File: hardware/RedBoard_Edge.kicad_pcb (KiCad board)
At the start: 2 copper layers, 101.6 x 38.1 mm, 67 parts, among them IC3 LM1117, J1 CONN_025MM, J17 Qwiic_Connector, J18 Qwiic_Connector, J2 ICSP, J3 POWER_JACKSUPER_BOMB_DIGITY, J4 microB, J5 CONN_04, J6 CONN_04, Q1 1A/60V/500mO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

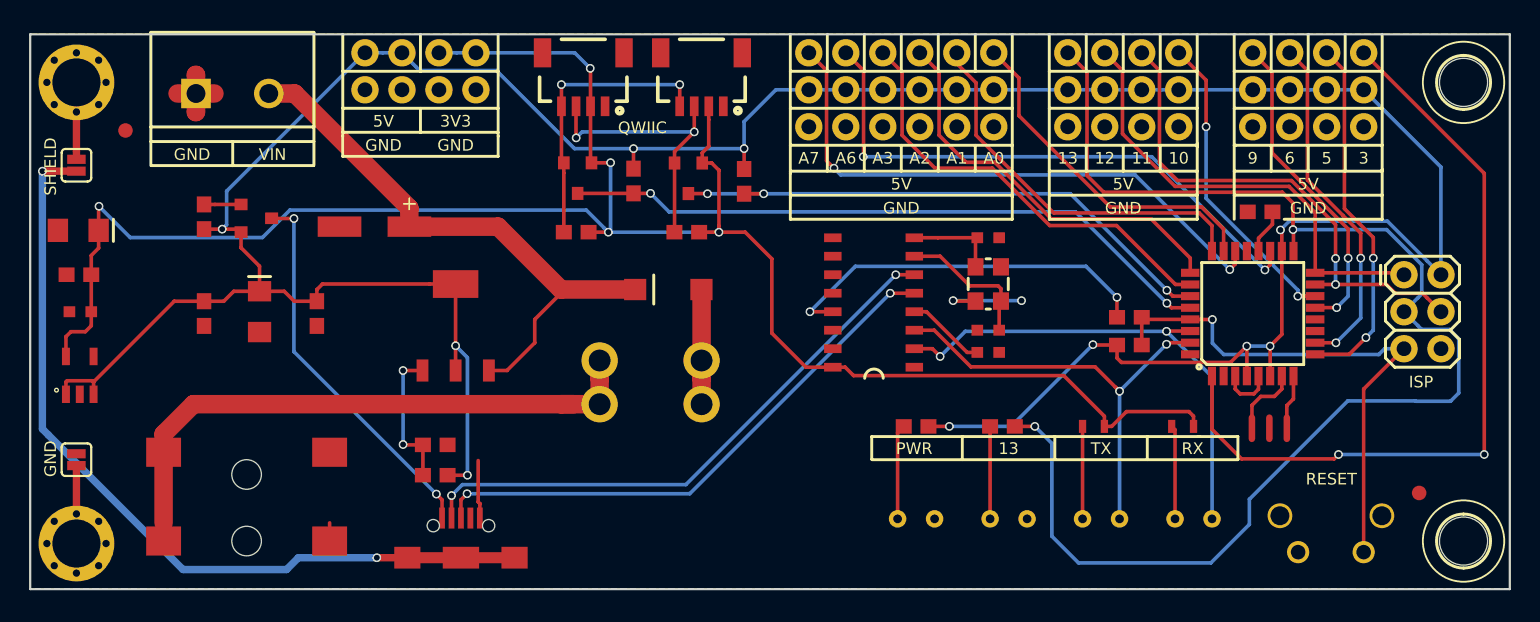
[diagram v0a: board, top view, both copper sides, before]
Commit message: Finalized Layout and ordered first run
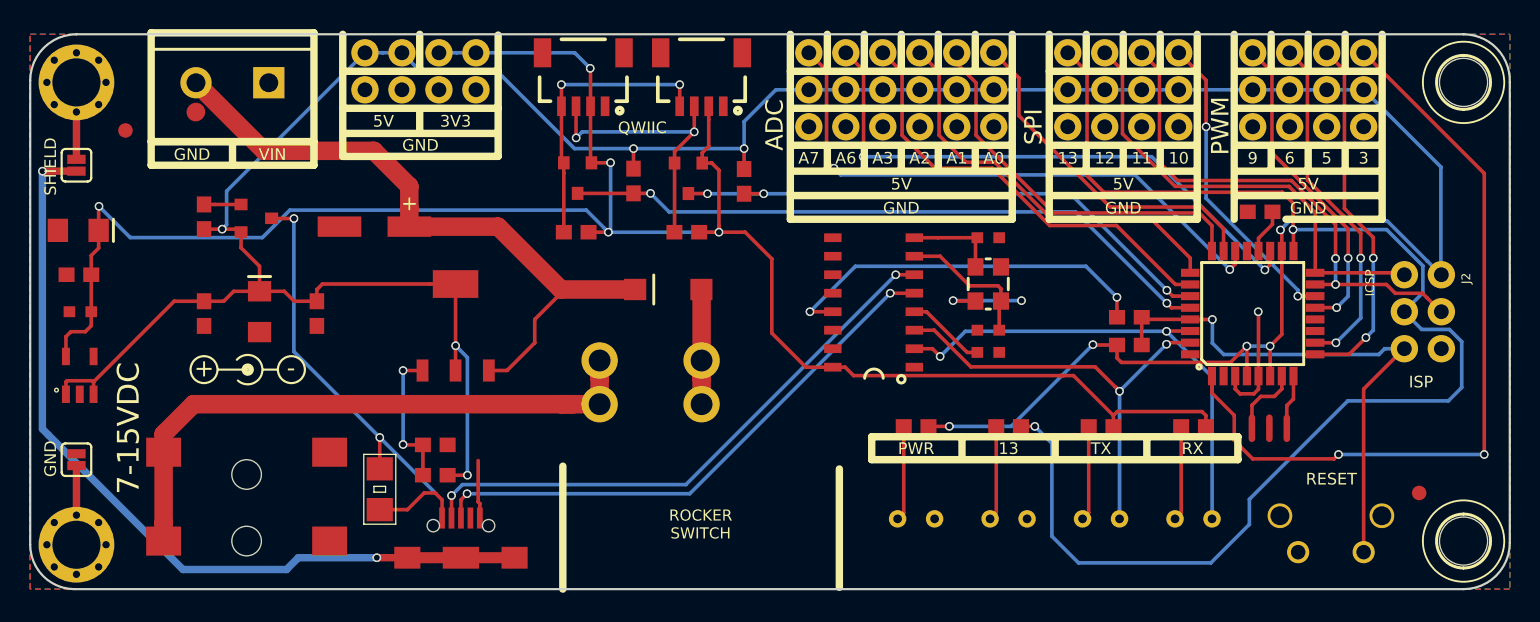
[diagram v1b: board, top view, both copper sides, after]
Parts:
- added F1: SPARKFUN-FUSES_PTC-HALF_AMP, RedBoard:SPARKFUN-FUSES_1206, F.Cu at (125.0, 110.5)
- added REF**: Symbol_Barrel_Polarity, Symbols:Symbol_Barrel_Polarity, F.Cu at (115.9, 102.3)
- J2: footprint Connectors:2X3 -> Connectors:2X3-NS
- R5, R6: footprint Resistors_SMD:R_0603 -> RedBoard:SPARKFUN-RESISTORS_0603
- moved J1 5.05 mm to (117.3, 82.6), turned to 180 degrees
- moved J2 2.85 mm to (196.6, 98.3)
- moved R5 0.75 mm to (180.8, 106.2)
- moved R6 0.52 mm to (174.5, 106.2)
- moved R1 0.42 mm to (168.1, 106.2)
- moved REF*** 0.13 mm to (115.0, 102.2)
- moved G*** 0.09 mm to (114.8, 92.0)
- moved U5 0.08 mm to (104.1, 114.3)
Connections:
- J4 pad VBUS: /USBVCC -> Net-(F1-Pad2)
- R4 pad 1: GND -> Net-(J3-PadGND)
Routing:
- net Net-(F1-Pad2): track 0.00 -> 6.20 mm
- net VIN: track 39.8 -> 46.0 mm
- net GND: track 22.9 -> 20.2 mm, vias 2 -> 3
- net 3.3V: track 135.4 -> 136.2 mm
- net Net-(J3-PadGND): track 0.00 -> 0.75 mm
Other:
- outline, holes or cut-outs redrawn
- board text added: "+"
- board text added: "-"
- board text added: "7-15VDC"
- board text added: "ADC"
- board text added: "PWM"
- board text added: "ROCKER SWITCH"
- board text added: "SPI"

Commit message: Fixed VIN Silk
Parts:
- F1: value SPARKFUN-FUSES_PTC-HALF_AMP -> PTC .5A
- Q2, Q3: value MOSFET-NCH-BSS138 -> BSS138
